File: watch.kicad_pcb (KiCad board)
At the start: 2 copper layers, 38 x 38 mm, 99 parts, among them IC1 IS32FL3237-TQLA3-TR, IC2 TMUX1237DCKR, Q1 RU1C002UNTCL, SW1 ButtonWakeup, SW2 ButtonUp, SW3 ButtonDown, U1 STM32L031F4Px, Y1 CR_32kHz

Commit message: V2 PCB first draft
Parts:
- removed IC1: IS32FL3237-TQLA3-TR, SamacSys_Parts:QFP50P900X900X120-49N
- removed IC2: TMUX1237DCKR, SamacSys_Parts:SOT65P210X110-6N
- removed R24: 3.8k, custom:R_0603_1608Metric
- removed R45, R46, R51: 10k, custom:R_0603_1608Metric
- removed SW1: ButtonWakeup, Button_Switch_SMD:SW_Push_1P1T-MP_NO_Horizontal_Alps_SKRTLAE010
- removed SW2: ButtonUp, Button_Switch_SMD:SW_Push_1P1T-MP_NO_Horizontal_Alps_SKRTLAE010
- removed SW3: ButtonDown, Button_Switch_SMD:SW_Push_1P1T-MP_NO_Horizontal_Alps_SKRTLAE010
- removed VR1: XC9140331MR-G, mrab:SOT-25
- added C11: 10uF, Capacitor_SMD:C_0603_1608Metric, F.Cu at (95.1, 94.3)
- added C12: 22uF, Capacitor_SMD:C_0603_1608Metric, F.Cu at (98.5, 88.2)
- added C13: 100nF, Capacitor_SMD:C_0603_1608Metric, F.Cu at (108.5, 98.2)
- added Q2: 2N7002H, Package_TO_SOT_SMD:SOT-23, B.Cu at (108.5, 89.0)
- added Q3: 2N7002H, Package_TO_SOT_SMD:SOT-23, B.Cu at (91.5, 89.0)
- added Q4: 2N7002H, Package_TO_SOT_SMD:SOT-23, B.Cu at (89.0, 91.5)
- added R10: 330/660, Resistor_SMD:R_0603_1608Metric_Pad0.98x0.95mm_HandSolder, B.Cu at (106.5, 87.5)
- added R11: 330/660, Resistor_SMD:R_0603_1608Metric_Pad0.98x0.95mm_HandSolder, B.Cu at (93.5, 87.5)
- added R12: 330/660, Resistor_SMD:R_0603_1608Metric_Pad0.98x0.95mm_HandSolder, B.Cu at (87.5, 93.5)
- added R13: 10K, Resistor_SMD:R_0603_1608Metric_Pad0.98x0.95mm_HandSolder, B.Cu at (100.8, 89.3)
- added R14: 10K, Resistor_SMD:R_0603_1608Metric_Pad0.98x0.95mm_HandSolder, B.Cu at (102.2, 89.3)
- added R15: 10K, Resistor_SMD:R_0603_1608Metric_Pad0.98x0.95mm_HandSolder, B.Cu at (97.8, 89.3)
- added R16: 10K, Resistor_SMD:R_0603_1608Metric_Pad0.98x0.95mm_HandSolder, B.Cu at (99.2, 89.3)
- added R17: 10K, Resistor_SMD:R_0603_1608Metric_Pad0.98x0.95mm_HandSolder, B.Cu at (100.8, 86.0)
- added R18: 10K, Resistor_SMD:R_0603_1608Metric_Pad0.98x0.95mm_HandSolder, B.Cu at (102.2, 86.0)
- added R19: 10K, Resistor_SMD:R_0603_1608Metric_Pad0.98x0.95mm_HandSolder, B.Cu at (97.8, 86.0)
- added R21: 16.2K, Resistor_SMD:R_0603_1608Metric_Pad0.98x0.95mm_HandSolder, F.Cu at (99.7, 89.2)
- added R22: 1.87K, Resistor_SMD:R_0603_1608Metric_Pad0.98x0.95mm_HandSolder, F.Cu at (100.8, 90.3)
- added R23: 36.5K, Resistor_SMD:R_0603_1608Metric_Pad0.98x0.95mm_HandSolder, F.Cu at (101.8, 91.4)
- added R9: 330/660, Resistor_SMD:R_0603_1608Metric_Pad0.98x0.95mm_HandSolder, B.Cu at (112.5, 93.5)
- added U2: ~, Package_LGA:LGA-12_2x2mm_P0.5mm, F.Cu at (100.0, 108.0)
- added U3: TPS63900, Package_SON:WSON-10-1EP_2.5x2.5mm_P0.5mm_EP1.2x2mm_ThermalVias, F.Cu at (96.5, 92.3)
- BT1: value CR2032_Battery -> CR2016_Battery; footprint SamacSys_Parts:BATHLD001 -> custom_lib:BatteryHolder_CR2016
- C1, C10: footprint custom:C_0603_1608Metric -> Capacitor_SMD:C_0603_1608Metric; moved to F.Cu
- C2: value 4.7uF -> 100nF; footprint custom:C_0603_1608Metric -> Capacitor_SMD:C_0603_1608Metric; moved to F.Cu
- C3: value 1uF -> 10uF; footprint custom:C_0603_1608Metric -> Capacitor_SMD:C_0603_1608Metric
- C4: footprint custom:C_0603_1608Metric -> Capacitor_SMD:C_0603_1608Metric
- C5: value 10uF -> 100nF; footprint custom:C_0603_1608Metric -> Capacitor_SMD:C_0603_1608Metric; moved to F.Cu
- C6, C7: value 100nF -> 15pF; footprint custom:C_0603_1608Metric -> Capacitor_SMD:C_0603_1608Metric; moved to F.Cu
- C8, C9: value 15pF -> 100nF; footprint custom:C_0603_1608Metric -> Capacitor_SMD:C_0603_1608Metric; moved to F.Cu
- D1, D10, D11, D12, D13, D14, D15, D16, D17, D18, D19, D2, D20, D21, D22, D23, D24, D25, D26, D27, D28, D29, D3, D30, D31, D32, D33, D34, D35, D36, D37, D38, D39, D4, D40, D41, D42, D43, D44, D45, D46, D47, D48, D49, D5, D50, D51, D52, D53, D54, D55, D56, D57, D58, D59, D6, D60, D7, D8, D9: value LED_Small -> LED; footprint custom:LED_0603_1608Metric -> custom_lib:LED_0603_1608Metric_Pad1.05x0.95mm_HandSolder
- L1: value 4.7uH -> 2.2uH; moved to F.Cu
- Q1: value RU1C002UNTCL -> 2N7002H; footprint mrab:SOT-323FL -> Package_TO_SOT_SMD:SOT-23
- R1, R2, R3: footprint custom:R_0603_1608Metric -> Resistor_SMD:R_0603_1608Metric_Pad0.98x0.95mm_HandSolder
- R20: value 100k -> 10K; footprint custom:R_0603_1608Metric -> Resistor_SMD:R_0603_1608Metric_Pad0.98x0.95mm_HandSolder; moved to B.Cu
- R4: value 10k -> 10M; footprint custom:R_0603_1608Metric -> Resistor_SMD:R_0603_1608Metric_Pad0.98x0.95mm_HandSolder; moved to F.Cu
- R5, R8: value 2k -> 10K; footprint custom:R_0603_1608Metric -> Resistor_SMD:R_0603_1608Metric_Pad0.98x0.95mm_HandSolder; moved to F.Cu
- R6: footprint custom:R_0603_1608Metric -> Resistor_SMD:R_0603_1608Metric_Pad0.98x0.95mm_HandSolder; moved to F.Cu
- R7: value 10k -> 2k; footprint custom:R_0603_1608Metric -> Resistor_SMD:R_0603_1608Metric_Pad0.98x0.95mm_HandSolder; moved to F.Cu
- TP1: value SWD_BAT -> SWD_nRST; footprint TestPoint:TestPoint_Pad_D2.0mm -> TestPoint:TestPoint_Pad_D1.0mm
- TP2: value SWD_GND -> SWD_CLK; footprint TestPoint:TestPoint_Pad_D2.0mm -> TestPoint:TestPoint_Pad_D1.0mm
- TP3: footprint TestPoint:TestPoint_Pad_D2.0mm -> TestPoint:TestPoint_Pad_D1.0mm
- TP4: value SWD_CLK -> SWD_GND; footprint TestPoint:TestPoint_Pad_D2.0mm -> TestPoint:TestPoint_Pad_D1.0mm
- TP5: value SWD_nRST -> SWD_BAT; footprint TestPoint:TestPoint_Pad_D2.0mm -> TestPoint:TestPoint_Pad_D1.0mm
- U1: value STM32L031F4Px -> STM32L071CBTx; footprint Package_SO:TSSOP-20_4.4x6.5mm_P0.65mm -> Package_QFP:LQFP-48_7x7mm_P0.5mm; moved to F.Cu
- Y1: moved to F.Cu
- moved D52 31.0 mm to (84.3, 103.3)
- moved D21 31.0 mm to (115.2, 95.0)
- moved D51 31.0 mm to (84.8, 104.9)
- moved D22 31.0 mm to (115.6, 96.6)
- moved D54 30.3 mm to (84.0, 99.9), turned to 0 degrees
- moved D19 30.3 mm to (113.8, 91.9), turned to -150 degrees
- moved D50 30.3 mm to (85.4, 106.4), turned to 24 degrees
- moved D23 30.3 mm to (115.9, 98.3), turned to -174 degrees
- moved D53 30.3 mm to (84.1, 101.6), turned to 6 degrees
- moved D20 30.3 mm to (114.6, 93.4), turned to -156 degrees
- moved D49 30.3 mm to (86.1, 107.9), turned to 30 degrees
- moved D24 30.3 mm to (116.0, 99.9), turned to 180 degrees
- moved TP1 30.2 mm to (86.2, 95.0)
- moved D56 28.3 mm to (84.3, 96.6), turned to -12 degrees
- moved D17 28.3 mm to (111.9, 89.2), turned to -138 degrees
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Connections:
- C1 pad 1: GND -> Net-(U1-PA5)
- C1 pad 2: nRST -> GND
- C10 pad 1: /LED_Driver/VCC_LED -> VDD
- C10 pad 2: GND1 -> GND
- C2 pad 1: +BATT -> GND
- C2 pad 2: GND1 -> nRST
- C3 pad 1: GND1 -> GND
- C3 pad 2: /LED_Driver/VCC_LED -> VDD
- C4 pad 1: GND1 -> GND
- C4 pad 2: /LED_Driver/VCC_LED -> VDD
- C5 pad 2: +BATT -> VDD
- C6 pad 1: GND -> Net-(U1-PC14)
- C6 pad 2: +BATT -> GND
- C7 pad 1: GND -> Net-(U1-PC15)
- C7 pad 2: +BATT -> GND
- C8 pad 1: Net-(C8-Pad1) -> VDD
- C9 pad 1: Net-(C9-Pad1) -> VDD
- D1 pad 1: Net-(D1-Pad1) -> Net-(D1-K)
- D1 pad 2: Net-(D1-Pad2) -> /LED_Matrix/LEDCOL0
- D10 pad 1: Net-(D10-Pad1) -> Net-(D10-K)
- D10 pad 2: Net-(D10-Pad2) -> /LED_Matrix/LEDCOL2
- D11 pad 1: Net-(D11-Pad1) -> Net-(D11-K)
- D11 pad 2: Net-(D1-Pad2) -> /LED_Matrix/LEDCOL2
- D12 pad 1: Net-(D11-Pad1) -> Net-(D12-K)
- D12 pad 2: Net-(D10-Pad2) -> /LED_Matrix/LEDCOL2
- D13 pad 1: Net-(D13-Pad1) -> Net-(D1-K)
- D13 pad 2: Net-(D1-Pad2) -> /LED_Matrix/LEDCOL3
- D14 pad 1: Net-(D13-Pad1) -> Net-(D10-K)
- D14 pad 2: Net-(D10-Pad2) -> /LED_Matrix/LEDCOL3
- D15 pad 1: Net-(D15-Pad1) -> Net-(D11-K)
- D15 pad 2: Net-(D1-Pad2) -> /LED_Matrix/LEDCOL3
- D16 pad 1: Net-(D15-Pad1) -> Net-(D12-K)
- D16 pad 2: Net-(D10-Pad2) -> /LED_Matrix/LEDCOL3
- D17 pad 1: Net-(D17-Pad1) -> Net-(D1-K)
- D17 pad 2: Net-(D1-Pad2) -> /LED_Matrix/LEDCOL4
- D18 pad 1: Net-(D17-Pad1) -> Net-(D10-K)
- D18 pad 2: Net-(D10-Pad2) -> /LED_Matrix/LEDCOL4
- D19 pad 1: Net-(D19-Pad1) -> Net-(D11-K)
- D19 pad 2: Net-(D1-Pad2) -> /LED_Matrix/LEDCOL4
- D2 pad 1: Net-(D1-Pad1) -> Net-(D10-K)
- D2 pad 2: Net-(D10-Pad2) -> /LED_Matrix/LEDCOL0
- D20 pad 1: Net-(D19-Pad1) -> Net-(D12-K)
- D20 pad 2: Net-(D10-Pad2) -> /LED_Matrix/LEDCOL4
- D21 pad 1: Net-(D21-Pad1) -> Net-(D1-K)
- D21 pad 2: Net-(D1-Pad2) -> /LED_Matrix/LEDCOL5
- D22 pad 1: Net-(D21-Pad1) -> Net-(D10-K)
- D22 pad 2: Net-(D10-Pad2) -> /LED_Matrix/LEDCOL5
- D23 pad 1: Net-(D23-Pad1) -> Net-(D11-K)
- D23 pad 2: Net-(D1-Pad2) -> /LED_Matrix/LEDCOL5
- D24 pad 1: Net-(D23-Pad1) -> Net-(D12-K)
- D24 pad 2: Net-(D10-Pad2) -> /LED_Matrix/LEDCOL5
- D25 pad 1: Net-(D25-Pad1) -> Net-(D1-K)
- D25 pad 2: Net-(D1-Pad2) -> /LED_Matrix/LEDCOL6
- D26 pad 1: Net-(D25-Pad1) -> Net-(D10-K)
- D26 pad 2: Net-(D10-Pad2) -> /LED_Matrix/LEDCOL6
- D27 pad 1: Net-(D27-Pad1) -> Net-(D11-K)
- D27 pad 2: Net-(D1-Pad2) -> /LED_Matrix/LEDCOL6
- D28 pad 1: Net-(D27-Pad1) -> Net-(D12-K)
- D28 pad 2: Net-(D10-Pad2) -> /LED_Matrix/LEDCOL6
- D29 pad 1: Net-(D29-Pad1) -> Net-(D1-K)
- D29 pad 2: Net-(D1-Pad2) -> /LED_Matrix/LEDCOL7
- D3 pad 1: Net-(D3-Pad1) -> Net-(D11-K)
- D3 pad 2: Net-(D1-Pad2) -> /LED_Matrix/LEDCOL0
- D30 pad 1: Net-(D29-Pad1) -> Net-(D10-K)
- D30 pad 2: Net-(D10-Pad2) -> /LED_Matrix/LEDCOL7
- D31 pad 1: Net-(D31-Pad1) -> Net-(D11-K)
- D31 pad 2: Net-(D1-Pad2) -> /LED_Matrix/LEDCOL7
- D32 pad 1: Net-(D31-Pad1) -> Net-(D12-K)
- D32 pad 2: Net-(D10-Pad2) -> /LED_Matrix/LEDCOL7
- D33 pad 1: Net-(D33-Pad1) -> Net-(D1-K)
- D33 pad 2: Net-(D1-Pad2) -> /LED_Matrix/LEDCOL8
- D34 pad 1: Net-(D33-Pad1) -> Net-(D10-K)
- D34 pad 2: Net-(D10-Pad2) -> /LED_Matrix/LEDCOL8
- D35 pad 1: Net-(D35-Pad1) -> Net-(D11-K)
- D35 pad 2: Net-(D1-Pad2) -> /LED_Matrix/LEDCOL8
- D36 pad 1: Net-(D35-Pad1) -> Net-(D12-K)
- D36 pad 2: Net-(D10-Pad2) -> /LED_Matrix/LEDCOL8
- D37 pad 1: Net-(D37-Pad1) -> Net-(D1-K)
- D37 pad 2: Net-(D1-Pad2) -> /LED_Matrix/LEDCOL9
- D38 pad 1: Net-(D37-Pad1) -> Net-(D10-K)
- D38 pad 2: Net-(D10-Pad2) -> /LED_Matrix/LEDCOL9
- D39 pad 1: Net-(D39-Pad1) -> Net-(D11-K)
- D39 pad 2: Net-(D1-Pad2) -> /LED_Matrix/LEDCOL9
- D4 pad 1: Net-(D3-Pad1) -> Net-(D12-K)
- D4 pad 2: Net-(D10-Pad2) -> /LED_Matrix/LEDCOL0
- D40 pad 1: Net-(D39-Pad1) -> Net-(D12-K)
- D40 pad 2: Net-(D10-Pad2) -> /LED_Matrix/LEDCOL9
- D41 pad 1: Net-(D41-Pad1) -> Net-(D1-K)
- D41 pad 2: Net-(D1-Pad2) -> /LED_Matrix/LEDCOL10
- D42 pad 1: Net-(D41-Pad1) -> Net-(D10-K)
- D42 pad 2: Net-(D10-Pad2) -> /LED_Matrix/LEDCOL10
- D43 pad 1: Net-(D43-Pad1) -> Net-(D11-K)
- D43 pad 2: Net-(D1-Pad2) -> /LED_Matrix/LEDCOL10
- D44 pad 1: Net-(D43-Pad1) -> Net-(D12-K)
- D44 pad 2: Net-(D10-Pad2) -> /LED_Matrix/LEDCOL10
- D45 pad 1: Net-(D45-Pad1) -> Net-(D1-K)
- D45 pad 2: Net-(D1-Pad2) -> /LED_Matrix/LEDCOL11
- D46 pad 1: Net-(D45-Pad1) -> Net-(D10-K)
- D46 pad 2: Net-(D10-Pad2) -> /LED_Matrix/LEDCOL11
- D47 pad 1: Net-(D47-Pad1) -> Net-(D11-K)
- D47 pad 2: Net-(D1-Pad2) -> /LED_Matrix/LEDCOL11
- D48 pad 1: Net-(D47-Pad1) -> Net-(D12-K)
- D48 pad 2: Net-(D10-Pad2) -> /LED_Matrix/LEDCOL11
- D49 pad 1: Net-(D49-Pad1) -> Net-(D1-K)
- D49 pad 2: Net-(D1-Pad2) -> /LED_Matrix/LEDCOL12
- D5 pad 1: Net-(D5-Pad1) -> Net-(D1-K)
- D5 pad 2: Net-(D1-Pad2) -> /LED_Matrix/LEDCOL1
- D50 pad 1: Net-(D49-Pad1) -> Net-(D10-K)
- D50 pad 2: Net-(D10-Pad2) -> /LED_Matrix/LEDCOL12
- D51 pad 1: Net-(D51-Pad1) -> Net-(D11-K)
- D51 pad 2: Net-(D1-Pad2) -> /LED_Matrix/LEDCOL12
- D52 pad 1: Net-(D51-Pad1) -> Net-(D12-K)
- D52 pad 2: Net-(D10-Pad2) -> /LED_Matrix/LEDCOL12
- D53 pad 1: Net-(D53-Pad1) -> Net-(D1-K)
- D53 pad 2: Net-(D1-Pad2) -> /LED_Matrix/LEDCOL13
- D54 pad 1: Net-(D53-Pad1) -> Net-(D10-K)
- D54 pad 2: Net-(D10-Pad2) -> /LED_Matrix/LEDCOL13
- D55 pad 1: Net-(D55-Pad1) -> Net-(D11-K)
- D55 pad 2: Net-(D1-Pad2) -> /LED_Matrix/LEDCOL13
- D56 pad 1: Net-(D55-Pad1) -> Net-(D12-K)
- D56 pad 2: Net-(D10-Pad2) -> /LED_Matrix/LEDCOL13
- D57 pad 1: Net-(D57-Pad1) -> Net-(D1-K)
- D57 pad 2: Net-(D1-Pad2) -> /LED_Matrix/LEDCOL14
- D58 pad 1: Net-(D57-Pad1) -> Net-(D10-K)
- D58 pad 2: Net-(D10-Pad2) -> /LED_Matrix/LEDCOL14
- D59 pad 1: Net-(D59-Pad1) -> Net-(D11-K)
- D59 pad 2: Net-(D1-Pad2) -> /LED_Matrix/LEDCOL14
- D6 pad 1: Net-(D5-Pad1) -> Net-(D10-K)
- D6 pad 2: Net-(D10-Pad2) -> /LED_Matrix/LEDCOL1
- D60 pad 1: Net-(D59-Pad1) -> Net-(D12-K)
- D60 pad 2: Net-(D10-Pad2) -> /LED_Matrix/LEDCOL14
- D7 pad 1: Net-(D7-Pad1) -> Net-(D11-K)
- D7 pad 2: Net-(D1-Pad2) -> /LED_Matrix/LEDCOL1
- D8 pad 1: Net-(D7-Pad1) -> Net-(D12-K)
- D8 pad 2: Net-(D10-Pad2) -> /LED_Matrix/LEDCOL1
- D9 pad 1: Net-(D10-Pad1) -> Net-(D1-K)
- D9 pad 2: Net-(D1-Pad2) -> /LED_Matrix/LEDCOL2
- L1 pad 1: +BATT -> Net-(U3-LX2)
- Q1 pad 1: Net-(Q1-Pad1) -> Net-(Q1-G)
- Q1 pad 3: GND1 -> Net-(Q1-D)
- R1 pad 1: SWDIO -> nRST
- R20 pad 2: /LED_Driver/VCC_LED -> LEDROW3
- R3 pad 1: nRST -> SWDIO
- R4 pad 1: Net-(R4-Pad1) -> Net-(U1-PA5)
- R4 pad 2: GND -> +BATT
- R5 pad 1: /LED_Driver/SCL -> Net-(U1-BOOT0)
- R5 pad 2: +BATT -> GND
- R6 pad 1: /LED_Driver/SDA -> /Accel/ACCEL_SCL
- R6 pad 2: +BATT -> VDD
- R7 pad 1: Net-(IC2-Pad6) -> /Accel/ACCEL_SDA
- R7 pad 2: /LED_Driver/LED_BANK -> VDD
- R8 pad 1: Net-(Q1-Pad1) -> Net-(U2-CS)
- R8 pad 2: Net-(U1-Pad9) -> VDD
- TP1 pad 1: +BATT -> Net-(R1-Pad2)
- TP2 pad 1: GND -> Net-(R2-Pad2)
- TP3 pad 1: Net-(R1-Pad2) -> Net-(R3-Pad2)
- TP4 pad 1: Net-(R2-Pad2) -> GND
- TP5 pad 1: Net-(R3-Pad2) -> +BATT
- U1 pad 1: Net-(R4-Pad1) -> VDD
- U1 pad 10: /LED_Driver/LED_BANK -> /Accel/ACCEL_EVT1
- U1 pad 11: unconnected-(U1-Pad11) -> LEDROW0
- U1 pad 12: unconnected-(U1-Pad12) -> LEDROW1
- U1 pad 13: unconnected-(U1-Pad13) -> LEDROW2
- U1 pad 14: unconnected-(U1-Pad14) -> LEDROW3
- U1 pad 15: GND -> Net-(U1-PA5)
- U1 pad 16: +BATT -> unconnected-(U1-PA6-Pad16)
- U1 pad 17: /LED_Driver/SCL -> unconnected-(U1-PA7-Pad17)
- U1 pad 18: /LED_Driver/SDA -> /LED_Matrix/LEDCOL0
- U1 pad 19: SWDIO -> /LED_Matrix/LEDCOL1
- U1 pad 2: Net-(C8-Pad1) -> /Accel/ACCEL_EVT0
- U1 pad 20: SWDCLK -> /LED_Matrix/LEDCOL2
- U1 pad 3: Net-(C9-Pad1) -> Net-(U1-PC14)
- U1 pad 4: nRST -> Net-(U1-PC15)
- U1 pad 5: +BATT -> Net-(U1-BOOT0)
- U1 pad 6: Net-(R51-Pad1) -> Net-(U1-BOOT0)
- U1 pad 7: Net-(R45-Pad1) -> nRST
- U1 pad 8: Net-(R46-Pad1) -> GND
- U1 pad 9: Net-(U1-Pad9) -> VDD
- Y1 pad 1: Net-(C9-Pad1) -> Net-(U1-PC15)
- Y1 pad 2: Net-(C8-Pad1) -> Net-(U1-PC14)
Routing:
- net Net-(D1-Pad2): track 122.2 -> 0.00 mm, vias 1 -> 0
- net Net-(D10-Pad2): track 114.8 -> 0.00 mm, vias 1 -> 0
- net VDD: track 0.00 -> 103.8 mm, vias 0 -> 10
- net +BATT: track 161.0 -> 60.7 mm, vias 11 -> 6
- net GND1: track 81.6 -> 0.00 mm, vias 3 -> 0
- net /LED_Driver/VCC_LED: track 46.9 -> 0.00 mm, vias 4 -> 0
- net /LED_Matrix/LEDCOL9: track 0.00 -> 34.5 mm, vias 0 -> 2
- net Net-(R45-Pad1): track 32.6 -> 0.00 mm, vias 2 -> 0
- net /LED_Matrix/LEDCOL3: track 0.00 -> 32.2 mm, vias 0 -> 2
- net Net-(R51-Pad1): track 31.1 -> 0.00 mm
- net /LED_Matrix/LEDCOL10: track 0.00 -> 30.5 mm, vias 0 -> 2
- net /Accel/ACCEL_SDA: track 0.00 -> 30.1 mm, vias 0 -> 3
- net Net-(R46-Pad1): track 29.9 -> 0.00 mm
- net /LED_Matrix/LEDCOL11: track 0.00 -> 29.1 mm, vias 0 -> 2
- net /Accel/ACCEL_SCL: track 0.00 -> 28.9 mm, vias 0 -> 2
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- added copper zone on F.Cu, net VDD
- removed copper zone on F.Cu, net GND
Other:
- board text removed: "3V3"
- board text removed: "GND"
- board text removed: "JLCJLCJLCJLC"
- board text removed: "SWDCLK"
- board text removed: "SWDIO"
- board text removed: "SWDRST"
- board text removed: "V1.4"

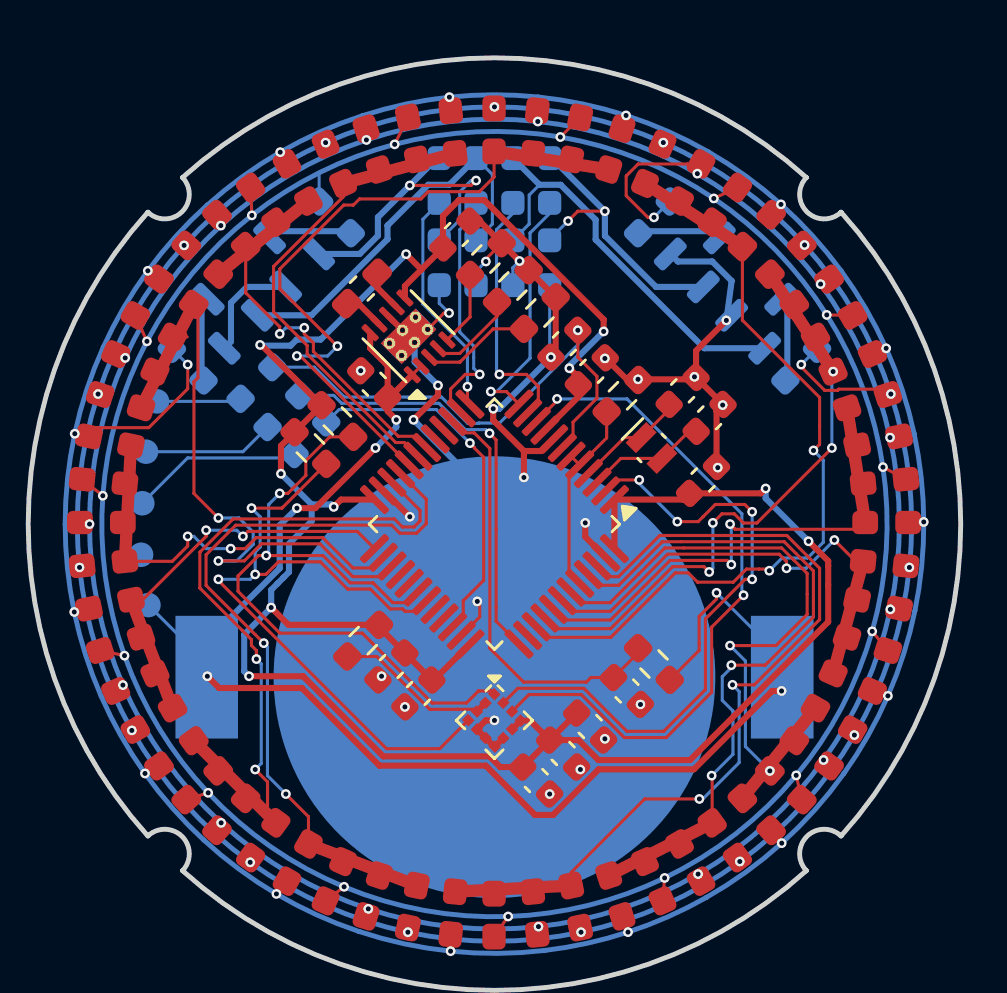
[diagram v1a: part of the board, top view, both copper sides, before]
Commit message: cleaned up silkscreen
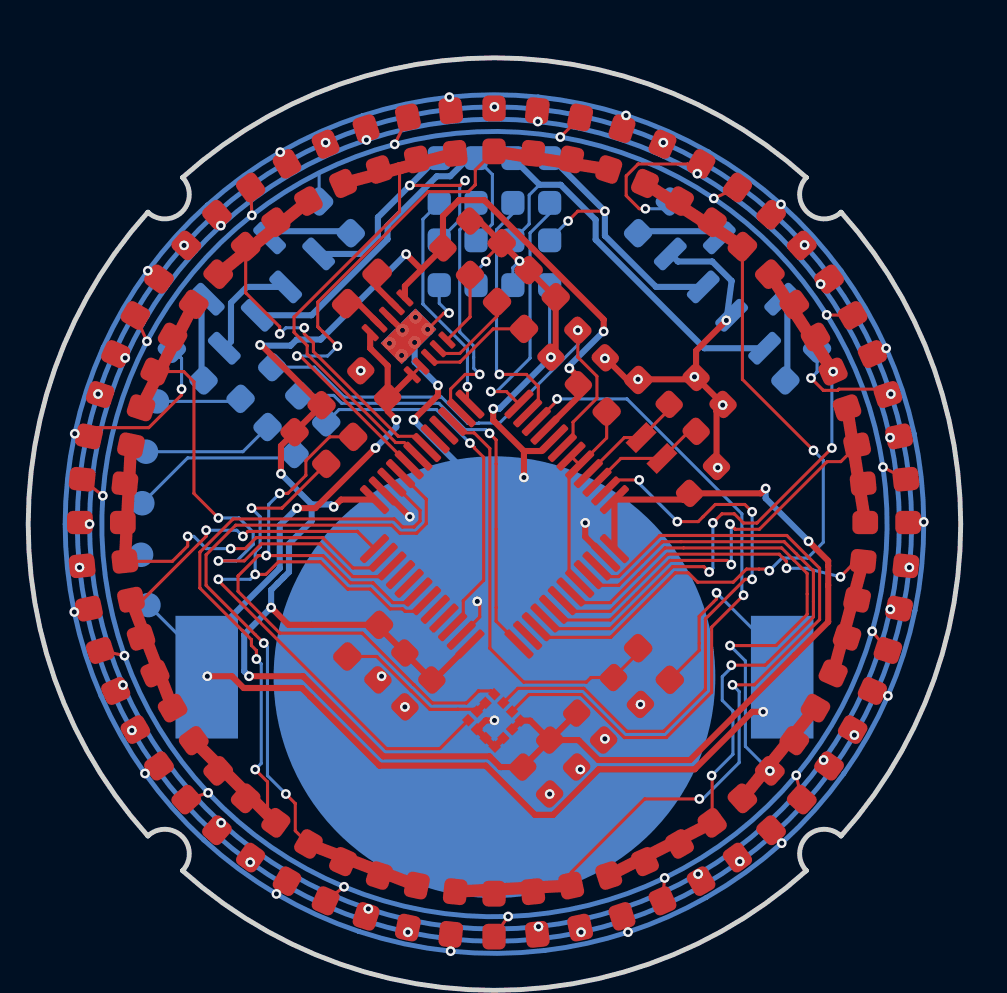
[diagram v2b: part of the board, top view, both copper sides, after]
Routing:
- net /LED_Matrix/LEDCOL2: track 28.5 -> 25.3 mm
- net /LED_Matrix/LEDCOL14: track 27.2 -> 25.3 mm
- net /LED_Matrix/LEDCOL5: track 21.2 -> 22.6 mm
- net +BATT: track 60.7 -> 59.6 mm
- net /LED_Matrix/LEDCOL1: track 19.7 -> 20.6 mm
- net Net-(Q3-G): track 13.1 -> 12.4 mm
- net /LED_Matrix/LEDCOL6: track 19.4 -> 18.8 mm

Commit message: PCB V2
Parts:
- added C14: 10uF, Capacitor_SMD:C_0603_1608Metric, F.Cu at (103.0, 90.7)
- added C15: 22uF, Capacitor_SMD:C_0603_1608Metric, F.Cu at (97.4, 92.7)
- added R24: 1K8, Resistor_SMD:R_0603_1608Metric_Pad0.98x0.95mm_HandSolder, F.Cu at (92.4, 98.1)
- added R25: 39K, Resistor_SMD:R_0603_1608Metric_Pad0.98x0.95mm_HandSolder, F.Cu at (102.0, 89.3)
- added R26: 560K, Resistor_SMD:R_0603_1608Metric_Pad0.98x0.95mm_HandSolder, F.Cu at (100.9, 88.2)
- C10, C11: value 10uF -> 100nF
- C12: value 22uF -> 100nF
- C13: value 100nF -> 10uF
- C2: moved to B.Cu
- R10, R11, R12, R9: value 330/660 -> 47
- R13, R14, R15, R16, R5, R8: value 10K -> 1M
- R21: value 16.2K -> 10K
- R22: value 1.87K -> 1M
- R23: value 36.5K -> 68
- R4: value 10M -> 1M
- R6, R7: value 2k -> 47K
- moved TP4 27.0 mm to (110.2, 90.1), turned to 45 degrees
- moved TP1 26.9 mm to (113.1, 93.1), turned to 45 degrees
- moved TP5 26.7 mm to (107.2, 87.2), turned to 45 degrees
- moved TP2 26.4 mm to (111.6, 91.6), turned to 45 degrees
- moved TP3 25.3 mm to (108.7, 88.7), turned to 45 degrees
- moved C12 21.5 mm to (102.8, 109.2), turned to -45 degrees
- moved R1 20.8 mm to (111.1, 95.0), turned to 45 degrees
- moved R9 19.8 mm to (93.9, 86.6), turned to -135 degrees
- moved R2 18.3 mm to (109.6, 93.5), turned to 45 degrees
- moved C11 16.4 mm to (103.8, 108.2), turned to -45 degrees
- moved Q1 15.4 mm to (95.8, 88.5), turned to 135 degrees
- moved R3 15.4 mm to (106.7, 90.5), turned to 45 degrees
- moved Q2 15.2 mm to (93.4, 91.0), turned to 135 degrees
- moved R10 15.1 mm to (91.4, 89.0), turned to -135 degrees
- moved R7 14.8 mm to (98.2, 110.5), turned to -135 degrees
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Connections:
- C10 pad 1: VDD -> GND
- C10 pad 2: GND -> VDD
- C11 pad 1: +BATT -> VDD
- C13 pad 1: GND -> VDD
- C13 pad 2: VDD -> GND
- C8 pad 1: VDD -> GND
- C8 pad 2: GND -> VDD
- C9 pad 1: VDD -> GND
- C9 pad 2: GND -> VDD
- R21 pad 1: GND -> /Power/SEL_VDD
- R21 pad 2: Net-(U3-CFG3) -> Net-(U3-SEL)
- R22 pad 1: GND -> Net-(U3-SEL)
- R22 pad 2: Net-(U3-CFG2) -> GND
- R23 pad 1: GND -> Net-(R23-Pad1)
- R23 pad 2: Net-(U3-CFG1) -> Net-(U3-CFG2)
- U1 pad 16: unconnected-(U1-PA6-Pad16) -> /Power/SEL_VDD
- U3 pad 2: +BATT -> Net-(U3-SEL)
- U3 pad 5: Net-(U3-CFG3) -> GND
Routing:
- net VDD: track 103.8 -> 42.3 mm, vias 10 -> 8
- net GND: track 62.1 -> 29.3 mm, vias 25 -> 28
- net +BATT: track 59.6 -> 36.6 mm, vias 6 -> 2
- net /Power/SEL_VDD: track 0.00 -> 16.6 mm, vias 0 -> 2
- net Net-(U3-SEL): track 0.00 -> 15.7 mm, vias 0 -> 2
- net /Accel/ACCEL_EVT1: track 28.5 -> 13.2 mm, vias 2 -> 0
- net Net-(U1-BOOT0): track 8.31 -> 21.5 mm, vias 0 -> 2
- net Net-(Q1-G): track 16.7 -> 3.78 mm
- net nRST: track 21.0 -> 9.89 mm
- net /LED_Matrix/LEDCOL7: track 27.0 -> 17.6 mm
- net Net-(U3-CFG2): track 3.69 -> 12.5 mm, vias 0 -> 2
- net /LED_Matrix/LEDCOL8: track 28.5 -> 20.6 mm
- net /LED_Matrix/LEDCOL0: track 17.3 -> 24.9 mm
- net /LED_Matrix/LEDCOL9: track 34.5 -> 27.4 mm
- net /Accel/ACCEL_EVT0: track 25.5 -> 19.0 mm, vias 4 -> 2
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- added copper zone on F.Cu, net GND
- added copper zone on In1.Cu, net GND
- added copper zone on In2.Cu, net VDD
- removed copper zone on B.Cu, net GND
- removed copper zone on F.Cu, net VDD
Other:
- copper layers 2 -> 4

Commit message: small fixes
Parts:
- added R27: 510, Resistor_SMD:R_0603_1608Metric_Pad0.98x0.95mm_HandSolder, B.Cu at (99.1, 92.9)
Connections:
- U3 pad 5: GND -> Net-(U3-CFG3)
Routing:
- net GND: track 29.3 -> 26.3 mm
- net Net-(U3-CFG3): track 0.00 -> 1.73 mm, vias 0 -> 1
- net VDD: track 42.3 -> 43.3 mm, vias 8 -> 9
- net LEDROW0: track 10.8 -> 11.6 mm

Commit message: good to go
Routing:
- net GND: track 26.3 -> 30.0 mm, vias 28 -> 30
- net VDD: vias 9 -> 8
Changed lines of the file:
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@@
 	)
 	(segment
+		(start 103.5 90.05)
+		(end 103.5 89.55953)
+		(width 0.5)
+		(layer "F.Cu")
+		(net 1)
+	)
+	(segment
 		(start 95.900586 99.082566)
 		(end 95.465678 98.647658)
@@
 	)
 	(segment
+		(start 103.5 90.053984)
+		(end 103.5 90.05)
+		(width 0.127)
+		(layer "F.Cu")
+		(net 1)
+	)
+	(segment
+		(start 103.5 90.05)
+		(end 103.496016 90.05)
+		(width 0.127)
+		(layer "F.Cu")
+		(net 1)
+	)
+	(segment
 		(start 105.122698 101.940718)
 		(end 105.122698 102.277302)
@@
 	(segment
 		(start 103.548008 90.101992)
-		(end 102.696016 89.25)
+		(end 103.5 90.053984)
 		(width 0.127)
 		(layer "F.Cu")
@@
 	)
 	(segment
+		(start 103.5 89.55953)
+		(end 102.645235 88.704765)
+		(width 0.5)
+		(layer "F.Cu")
+		(net 1)
+	)
+	(segment
 		(start 100.247487 92.247487)
 		(end 100.857367 92.857367)
@@
 	)
 	(segment
+		(start 102.645235 88.704765)
+		(end 101.545235 87.604765)
+		(width 0.5)
+		(layer "F.Cu")
+		(net 1)
+	)
+	(segment
 		(start 102.6 89.25)
 		(end 102.6 88.75)
@@
 	)
 	(segment
-		(start 102.645235 88.704765)
-		(end 101.545235 87.604765)
-		(width 0.127)
-		(layer "F.Cu")
-		(net 1)
-	)
-	(segment
 		(start 104.55 93.6)
 		(end 104.548008 93.601992)
@@
 	)
 	(via
+		(at 102.55 88.25)
+		(size 0.4)
+		(drill 0.2)
+		(layers "F.Cu" "B.Cu")
+		(net 1)
+	)
+	(via
 		(at 104.75 87.15)
 		(size 0.4)
@@
 		(net 1)
 	)
+	(via
+		(at 103.5 90.05)
+		(size 0.4)
+		(drill 0.2)
+		(layers "F.Cu" "B.Cu")
+		(net 1)
+	)
 	(segment
 		(start 99.049845 98.099845)
@@
 		(start 101.44922 90.44125)
 		(end 102.545235 89.345235)
-		(width 0.127)
+		(width 0.5)
+		(layer "B.Cu")
+		(net 1)
+	)
+	(segment
+		(start 102.545235 89.345235)
+		(end 103.641251 88.249219)
+		(width 0.5)
+		(layer "B.Cu")
+		(net 1)
+	)
+	(segment
+		(start 103.641251 88.249219)
+		(end 104.737266 87.153204)
+		(width 0.5)
 		(layer "B.Cu")
 		(net 1)
@@
 	)
 	(segment
-		(start 107.232753 87.182753)
-		(end 107.217247 87.182753)
-		(width 0.25)
-		(layer "B.Cu")
-		(net 2)
-	)
-	(segment
-		(start 103.65 90)
-		(end 102.451992 91.198008)
+		(start 112.569276 105.393224)
+		(end 112.569276 96.419276)
 		(width 0.25)
 		(layer "B.Cu")
@@
 	)
 	(segment
-		(start 89.2625 105.25)
-		(end 88.275 106.2375)
-		(width 0.127)
-		(layer "B.Cu")
-		(net 2)
-	)
-	(segment
 		(start 111.725 106.2375)
 		(end 112.569276 105.393224)
@@
 	)
 	(segment
-		(start 112.569276 96.422514)
-		(end 106.146762 90)
+		(start 103.217498 91.198008)
+		(end 105.282753 89.132753)
 		(width 0.25)
 		(layer "B.Cu")
@@
 	)
 	(segment
-		(start 106.146762 90)
-		(end 103.65 90)
+		(start 107.232753 87.182753)
+		(end 107.217247 87.182753)
 		(width 0.25)
 		(layer "B.Cu")
@@
 	)
 	(segment
-		(start 89.9 105.25)
-		(end 89.2625 105.25)
+		(start 89.2625 105.25)
+		(end 88.275 106.2375)
 		(width 0.127)
 		(layer "B.Cu")
@@
 	)
 	(segment
-		(start 112.569276 105.393224)
-		(end 112.569276 96.422514)
+		(start 112.569276 96.419276)
+		(end 105.282753 89.132753)
 		(width 0.25)
 		(layer "B.Cu")
@@
 	)
 	(segment
-		(start 107.217247 87.182753)
-		(end 106.146762 88.253238)
+		(start 105.282753 89.132753)
+		(end 107.232753 87.182753)
 		(width 0.25)
 		(layer "B.Cu")
@@
 	)
 	(segment
-		(start 106.146762 88.253238)
-		(end 106.146762 90)
+		(start 102.451992 91.198008)
+		(end 103.217498 91.198008)
 		(width 0.25)
 		(layer "B.Cu")
@@
 	)
 	(segment
+		(start 89.9 105.25)
+		(end 89.2625 105.25)
+		(width 0.127)
+		(layer "B.Cu")
+		(net 2)
+	)
+	(segment
 		(start 103.7 96.25)
 		(end 103.396446 96.25)
@@
 	)
 	(segment
-		(start 97.95 93.25)
-		(end 97.7 93.25)
-		(width 0.25)
-		(layer "F.Cu")
-		(net 4)
-	)
-	(segment
 		(start 106.701992 98.198008)
 		(end 106.7 98.2)
@@
 	)
 	(segment
-		(start 97.7 93.25)
-		(end 97.15 93.8)
-		(width 0.25)
-		(layer "F.Cu")
-		(net 4)
-	)
-	(segment
 		(start 93.99697 105.908)
 		(end 94.684205 106.595235)
@@
 	)
 	(segment
+		(start 97.2 93.75)
+		(end 97.7 93.25)
+		(width 0.25)
+		(layer "F.Cu")
+		(net 4)
+	)
+	(segment
 		(start 96.504766 110.045235)
 		(end 96.504765 110.045235)
@@
 		(net 4)
 	)
+	(segment
+		(start 97.7 93.25)
+		(end 97.95 93.25)
+		(width 0.25)
+		(layer "F.Cu")
+		(net 4)
+	)
 	(via
 		(at 107.8 100.75)
@@
 	)
 	(via
-		(at 97.95 93.25)
-		(size 0.4)
-		(drill 0.2)
-		(layers "F.Cu" "B.Cu")
-		(net 4)
-	)
-	(via
 		(at 106.7 98.2)
 		(size 0.4)
@@
 	)
 	(via
-		(at 97.15 93.8)
+		(at 97.2 93.75)
 		(size 0.4)
 		(drill 0.2)
@@
 	)
 	(segment
-		(start 96.15 95.15)
-		(end 96.26923 95.03077)
+		(start 98.21275 95.03077)
+		(end 98.647658 95.465678)
 		(width 0.127)
 		(layer "F.Cu")
@@
 	)
 	(segment
-		(start 96.26923 95.03077)
-		(end 98.21275 95.03077)
+		(start 96.15 95.15)
+		(end 96.26923 95.03077)
 		(width 0.127)
 		(layer "F.Cu")
@@
 	)
 	(segment
-		(start 98.21275 95.03077)
-		(end 98.647658 95.465678)
+		(start 96.26923 95.03077)
+		(end 98.21275 95.03077)
 		(width 0.127)
 		(layer "F.Cu")

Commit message: ready for ordering?
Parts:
- removed R21: 10K, Resistor_SMD:R_0603_1608Metric_Pad0.98x0.95mm_HandSolder
- removed R25: 39K, Resistor_SMD:R_0603_1608Metric_Pad0.98x0.95mm_HandSolder
- removed R26: 560K, Resistor_SMD:R_0603_1608Metric_Pad0.98x0.95mm_HandSolder
- R10, R11, R12, R9: value 47 -> 20
- Y1: footprint Crystal:Crystal_SMD_MicroCrystal_CM9V-T1A-2Pin_1.6x1.0mm -> Crystal:Crystal_SMD_MicroCrystal_CM9V-T1A-2Pin_1.6x1.0mm_HandSoldering
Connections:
- U1 pad 16: /Power/SEL_VDD -> unconnected-(U1-PA6-Pad16)
- U3 pad 3: Net-(U3-CFG1) -> GND
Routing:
- net +BATT: track 36.9 -> 62.3 mm
- net GND: track 30.0 -> 46.9 mm, vias 30 -> 28
- net /Power/SEL_VDD: track 16.6 -> 0.00 mm, vias 2 -> 0
- net Net-(U3-CFG1): track 5.81 -> 0.00 mm
- net VDD: track 43.3 -> 46.5 mm
- net Net-(U3-SEL): track 15.7 -> 13.9 mm
- net /LED_Matrix/LEDCOL1: track 25.7 -> 24.5 mm
- net /LED_Matrix/LEDCOL4: track 26.4 -> 25.8 mm
- added copper zone on B.Cu, net GND

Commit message: as ordered
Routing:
- net GND: track 46.9 -> 48.5 mm, vias 28 -> 27
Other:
- board text added: "CLK"
- board text added: "GND"
- board text added: "IO"
- board text added: "JLCJLCJLCJLC"
- board text added: "REV 1.5"
- board text added: "VDD"
- board text added: "nRST"
